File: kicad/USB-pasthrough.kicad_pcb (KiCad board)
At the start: 4 copper layers, 40 x 100 mm, 93 parts, among them J1 USB_Power, J10 MicroSD, J4 Power_Sel, J5 SPI Display, J6 SWD, J7 Cortex Debug, J8 USB_C, J9 USB_A, SW1 Boot0, SW2 Reset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

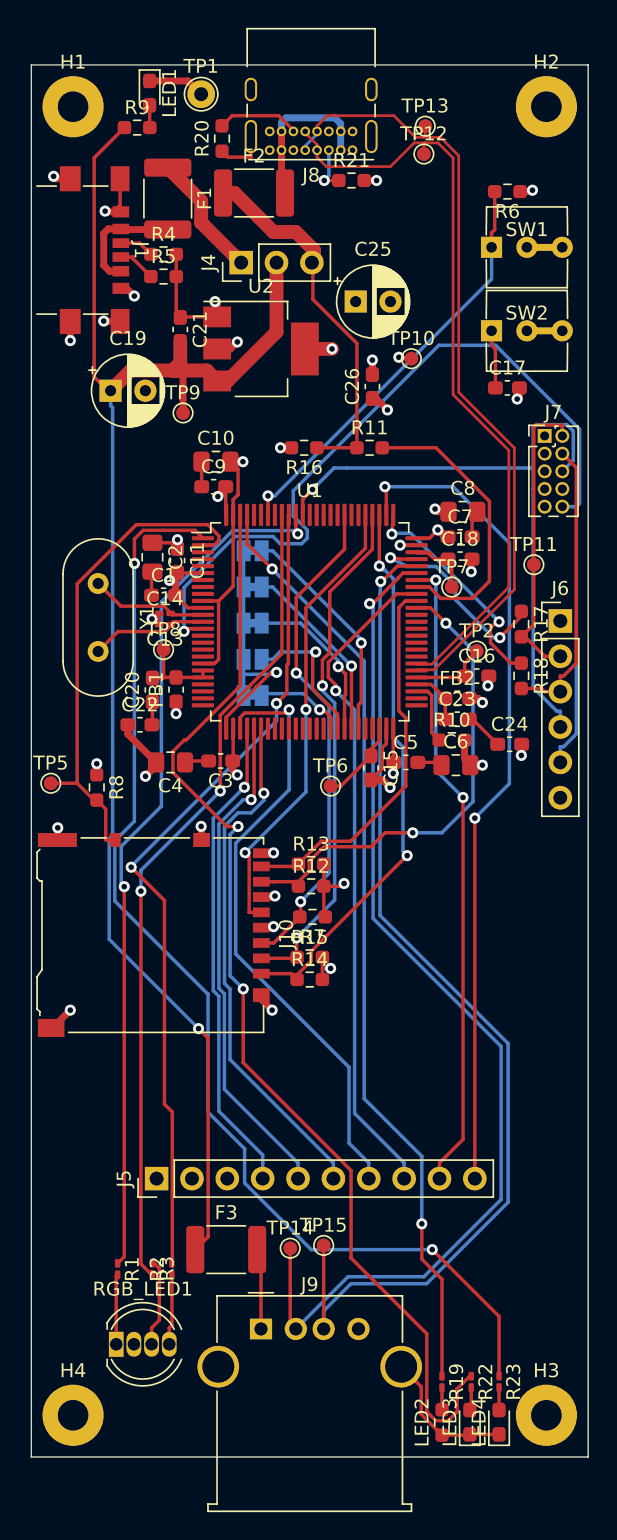
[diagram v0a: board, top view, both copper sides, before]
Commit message: Tweak PCB
1. Import LED2 footprint update
2. Move TP8
3. Adjust silkscreen
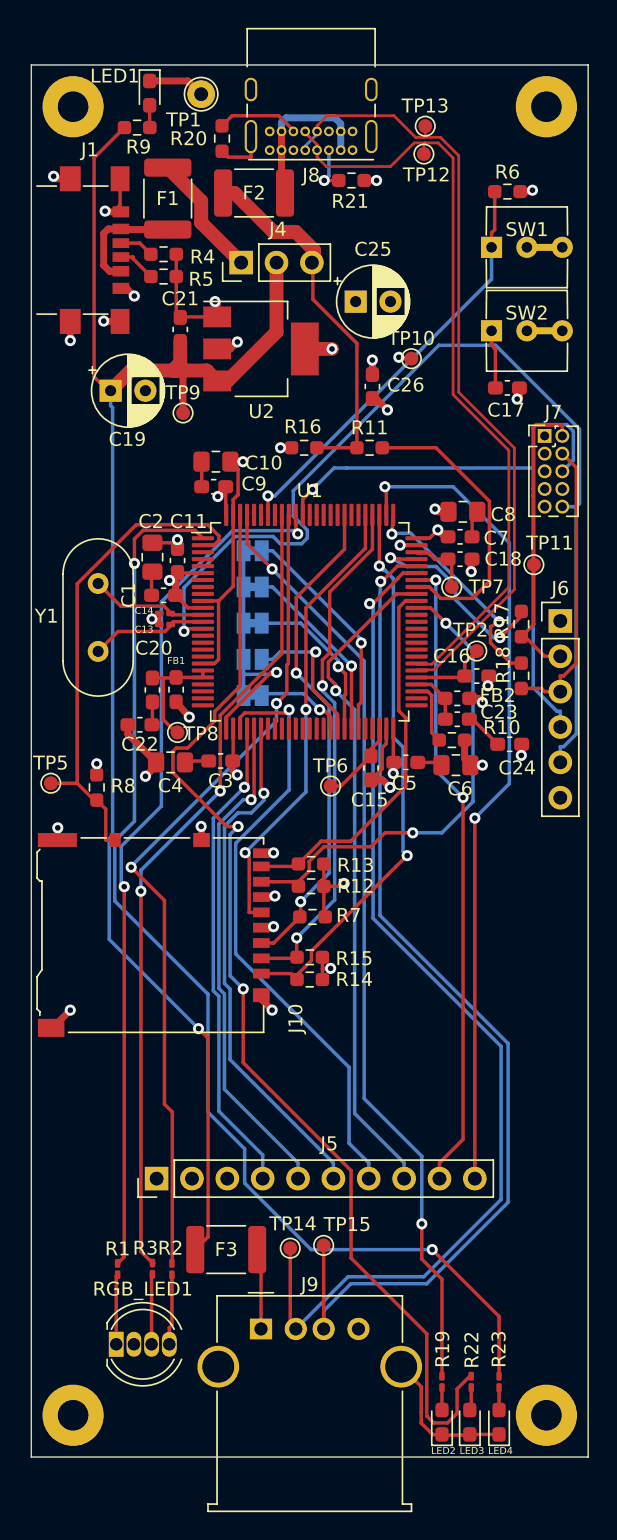
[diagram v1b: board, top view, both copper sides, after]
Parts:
- LED2: footprint Resistor_SMD:R_0603_1608Metric_Pad0.98x0.95mm_HandSolder -> LED_SMD:LED_0603_1608Metric_Pad1.05x0.95mm_HandSolder
- moved TP8 6.03 mm to (110.5, 98.0)
- turned R3 to 90 degrees
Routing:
- net /VDDA: track 6.14 -> 8.43 mm
- net Net-(R3-Pad1): track 6.34 -> 5.13 mm
- net /LED3: track 80.7 -> 81.5 mm
- net /LED5_B: track 59.1 -> 58.4 mm
- net +3V3: track 35.6 -> 36.2 mm

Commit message: Tweak PCB
1. adjust some signals
2. Increase the size of the +5V trace to the USBA connector
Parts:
- moved TP15 2.20 mm to (121.0, 137.0)
- moved TP14 2.01 mm to (118.8, 137.0)
- moved TP6 1.86 mm to (122.6, 100.3)
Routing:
- net /MMC1_CDET: track 35.8 -> 41.9 mm
- net GND: track 106.5 -> 103.0 mm, vias 29 -> 31
- net +5V: track 110.7 -> 113.9 mm
- net /LED5_G: track 59.7 -> 62.4 mm
- net /LED5_B: track 58.4 -> 60.7 mm
- net /USBA+: track 75.2 -> 73.0 mm
- net /VCAP_1: track 6.01 -> 4.32 mm
- net /LED5_R: track 62.4 -> 64.1 mm
- net /USBA-: track 75.6 -> 74.1 mm
- net /LED4: track 82.7 -> 84.0 mm
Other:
- board text added: "+3V3"
- board text added: "GND"
- board text added: "SWCLK"
- board text added: "SWDIO"
- board text added: "SWO"
- board text added: "nRST"

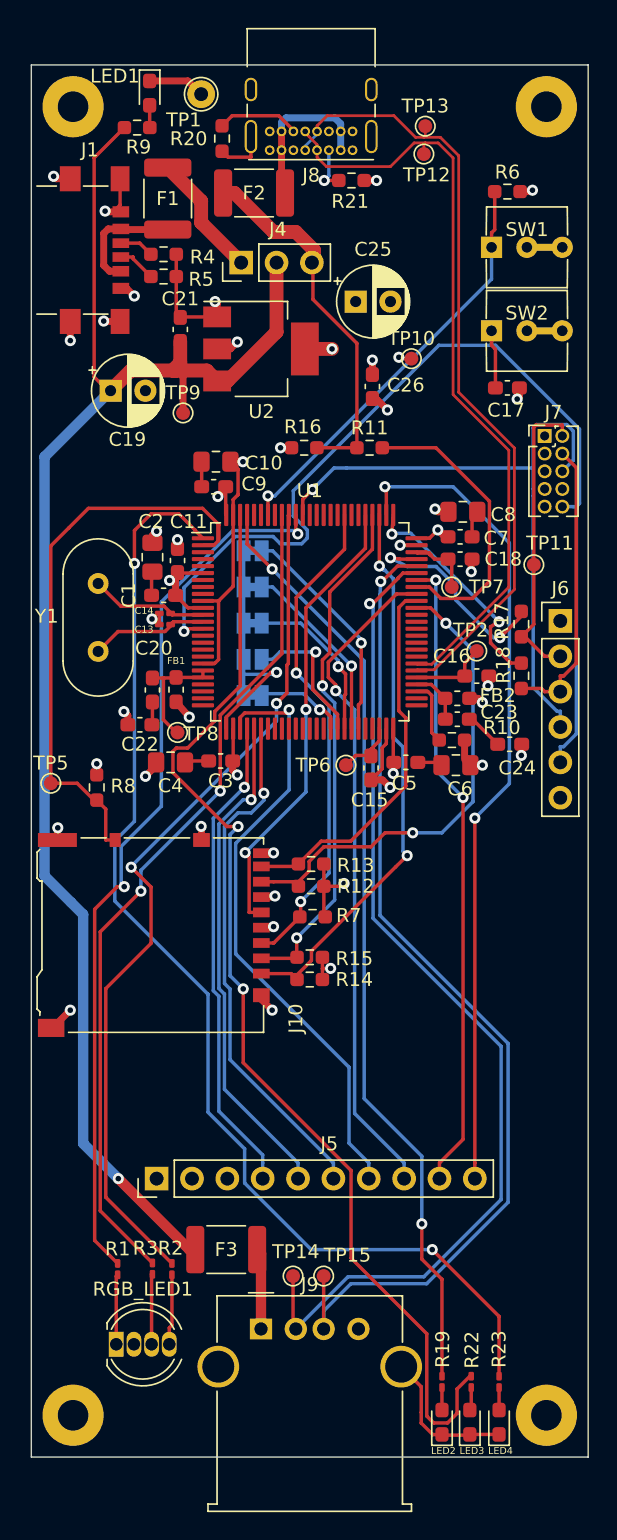
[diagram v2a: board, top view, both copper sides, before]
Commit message: Update PCB
1. Move SD socket to bottom of board (to reduce size of PCB)
2. Reduce size of PCB
3. reroute traces
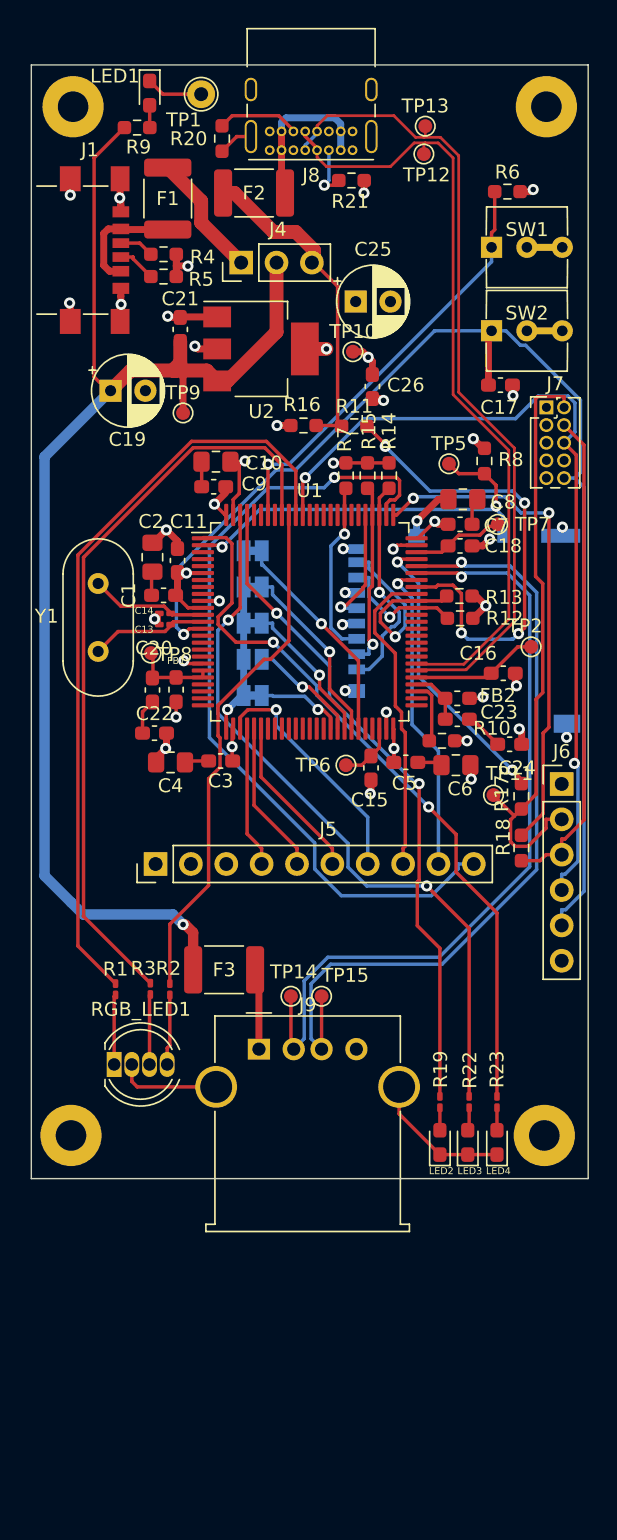
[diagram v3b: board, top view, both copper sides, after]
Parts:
- J10: moved to B.Cu
- moved TP5 36.7 mm to (130.0, 78.7)
- moved R14 36.6 mm to (125.7, 79.5), turned to 90 degrees
- moved R8 36.4 mm to (132.6, 78.5)
- moved R15 34.8 mm to (124.2, 79.5), turned to 90 degrees
- moved R7 31.8 mm to (122.6, 79.5), turned to -90 degrees
- moved J10 31.2 mm to (131.1, 90.7)
- moved J5 22.6 mm to (108.9, 107.4)
- moved R12 22.0 mm to (130.8, 89.8)
- moved R13 22.0 mm to (130.8, 88.2)
- moved J9 20.1 mm to (116.3, 120.7)
- moved RGB_LED1 20.1 mm to (106.0, 121.8)
- moved F3 20.1 mm to (113.8, 115.0)
- moved H3 20.1 mm to (136.8, 126.9)
- moved H4 20.1 mm to (102.8, 126.9)
- moved LED2 20.1 mm to (129.3, 127.4)
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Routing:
- net /LED4: track 84.0 -> 52.3 mm
- net /LED3: track 81.5 -> 52.4 mm
- net /LCD_CS: track 43.8 -> 17.4 mm
- net /SPI1_MOSI: track 37.4 -> 11.8 mm, vias 1 -> 0
- net /MMC1_D0: track 34.5 -> 9.06 mm, vias 2 -> 1
- net /LCD_DC: track 47.7 -> 22.7 mm, vias 1 -> 0
- net /SPI1_MISO: track 36.1 -> 11.0 mm, vias 1 -> 0
- net /LED5_G: track 62.4 -> 37.6 mm, vias 2 -> 0
- net /SPI1_SCK: track 34.8 -> 10.2 mm, vias 1 -> 0
- net /MMC1_D2: track 40.2 -> 15.8 mm, vias 2 -> 1
- net /MMC1_CLK: track 33.1 -> 8.70 mm, vias 2 -> 1
- net /MMC1_D3: track 37.3 -> 13.3 mm, vias 2 -> 1
- net /LCD_RST: track 45.9 -> 22.8 mm, vias 2 -> 1
- net /MMC1_CMD: track 35.7 -> 12.7 mm, vias 2 -> 1
- net /SWDIO: track 21.6 -> 43.0 mm
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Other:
- board size 40 x 100 mm -> 40 x 80 mm

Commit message: Tweak PCD and slikscreen
1. Reroute traces to clear Xtal footprint
2. Label pins on SWD header (move resistors)
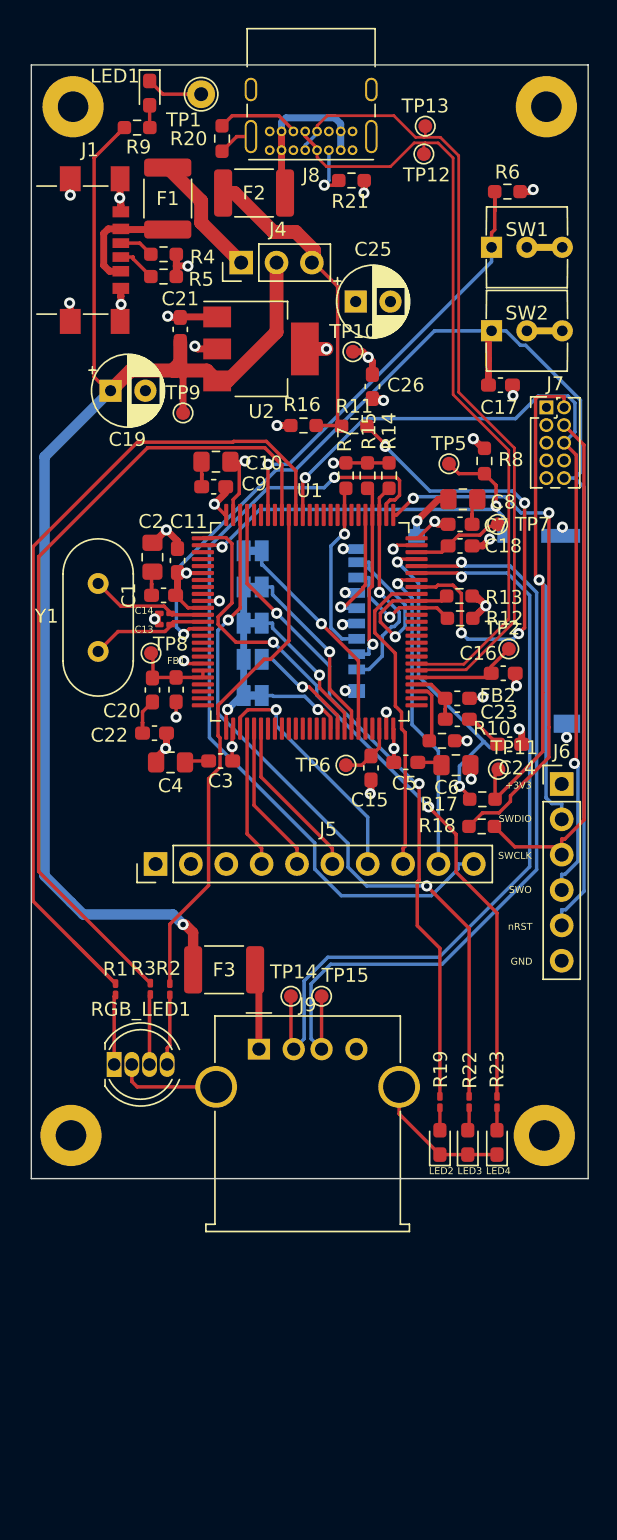
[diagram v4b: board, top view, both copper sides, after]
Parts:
- moved R18 3.24 mm to (132.3, 104.7), turned to 0 degrees
- moved R17 2.81 mm to (132.4, 102.8), turned to 0 degrees
- moved TP11 1.88 mm to (133.6, 100.6)
- moved TP2 1.61 mm to (134.3, 92.0)
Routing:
- net /SWDIO: track 43.0 -> 53.8 mm, vias 0 -> 1
- net /LED5_R: track 55.0 -> 64.1 mm
- net /LED5_B: track 54.2 -> 58.8 mm
- net /SWCLK: track 35.3 -> 37.7 mm
- net /PA13: track 21.1 -> 23.0 mm
- net /nRESET: track 88.4 -> 90.2 mm
- net GND: track 93.9 -> 95.7 mm
- net /PA14: track 36.2 -> 37.8 mm
- net /V12PHYHS: track 9.14 -> 7.76 mm
- net Net-(R6-Pad2): track 30.9 -> 32.2 mm
- net +3V3: track 33.5 -> 34.6 mm
- net Net-(C7-Pad2): track 1.96 -> 2.93 mm
- net Net-(C10-Pad1): track 1.81 -> 2.70 mm
- net Net-(C1-Pad1): track 1.73 -> 2.54 mm
- net Net-(C20-Pad1): track 2.53 -> 3.29 mm
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
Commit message: Realign pin 1 of components, up and left
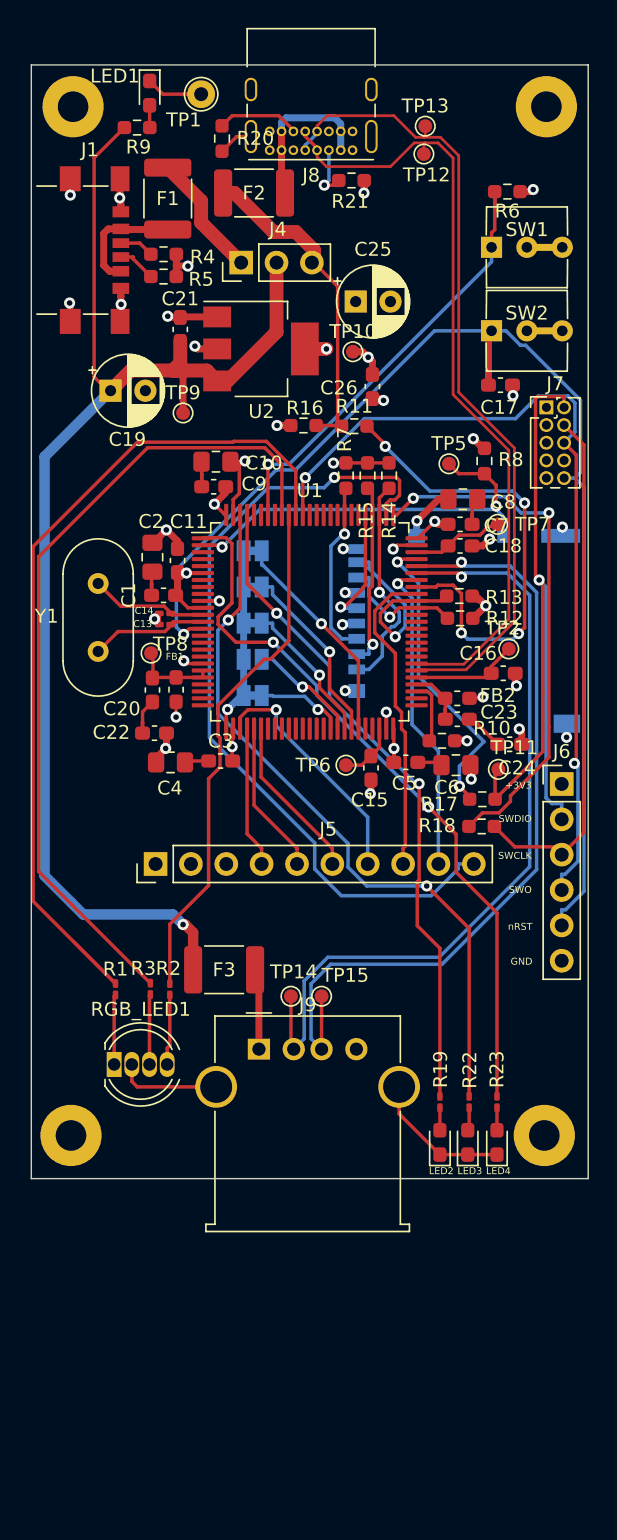
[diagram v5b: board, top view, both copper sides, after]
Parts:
- JP1: value ID0 -> Jumper_2_Bridged
- JP2: value ID1 -> Jumper_2_Bridged
- JP3: value ID2 -> Jumper_2_Bridged
- JP4: value ID3 -> Jumper_2_Bridged
- JP5: value ID4 -> Jumper_2_Bridged
- turned C13 to 0 degrees
- turned C20 to -90 degrees
- turned C22 to 0 degrees
- turned C26 to -90 degrees
- turned C3 to 0 degrees
- turned C4 to 0 degrees
- turned FB1 to -90 degrees
- turned R14 to -90 degrees
- turned R15 to -90 degrees
- turned R16 to 0 degrees
- turned R20 to -90 degrees
- turned R6 to 0 degrees
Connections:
- C13 pad 1: Net-(C13-Pad1) -> GND
- C13 pad 2: GND -> Net-(U1-Pad13)
- C20 pad 1: Net-(C20-Pad1) -> /VDDA
- C20 pad 2: /VDDA -> Net-(C20-Pad2)
- C22 pad 1: GND -> Net-(C20-Pad2)
- C22 pad 2: Net-(C20-Pad1) -> GND
- C26 pad 1: GND -> +3V3
- C26 pad 2: +3V3 -> GND
- C3 pad 1: +3V3 -> Net-(C4-Pad2)
- C3 pad 2: Net-(C3-Pad2) -> +3V3
- C4 pad 1: Net-(C3-Pad2) -> GND
- C4 pad 2: GND -> Net-(C4-Pad2)
- FB1 pad 1: +3V3 -> /VDDA
- FB1 pad 2: /VDDA -> +3V3
- R14 pad 1: /MMC1_D2 -> +3V3
- R14 pad 2: +3V3 -> /MMC1_D2
- R15 pad 1: /MMC1_D3 -> +3V3
- R15 pad 2: +3V3 -> /MMC1_D3
- R16 pad 1: /VBUS_DATA -> GND
- R16 pad 2: GND -> /VBUS_DATA
- R20 pad 1: GND -> Net-(J8-PadB5)
- R20 pad 2: Net-(J8-PadB5) -> GND
- R6 pad 1: GND -> Net-(SW1-Pad1)
- R6 pad 2: Net-(R6-Pad2) -> GND
- SW1 pad 1: Net-(R6-Pad2) -> Net-(SW1-Pad1)
- U1 pad 13: Net-(C13-Pad1) -> Net-(U1-Pad13)
- U1 pad 94: Net-(R6-Pad2) -> Net-(SW1-Pad1)
- Y1 pad 2: Net-(C13-Pad1) -> Net-(U1-Pad13)
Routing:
- net Net-(SW1-Pad1): track 0.00 -> 32.2 mm, vias 0 -> 1
- net Net-(R6-Pad2): track 32.2 -> 0.00 mm, vias 1 -> 0
- net Net-(U1-Pad13): track 0.00 -> 8.51 mm
- net Net-(C13-Pad1): track 8.51 -> 0.00 mm
- net Net-(C20-Pad2): track 0.00 -> 3.29 mm
- net Net-(C20-Pad1): track 3.29 -> 0.00 mm
- net Net-(C3-Pad2): track 1.81 -> 0.00 mm
- net Net-(C4-Pad2): track 0.00 -> 1.81 mm
- net /PA13: track 23.0 -> 21.9 mm
- net +5V: track 98.1 -> 97.4 mm
